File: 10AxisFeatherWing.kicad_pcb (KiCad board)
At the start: 2 copper layers, 50.8 x 22.9 mm, 28 parts, among them J1 feather long, J2 feather short, J4 feather long, J5 feather short, SW1 SW_Push_Dual, U1 BNO055, U2 BME280, Y1 32.768kHz

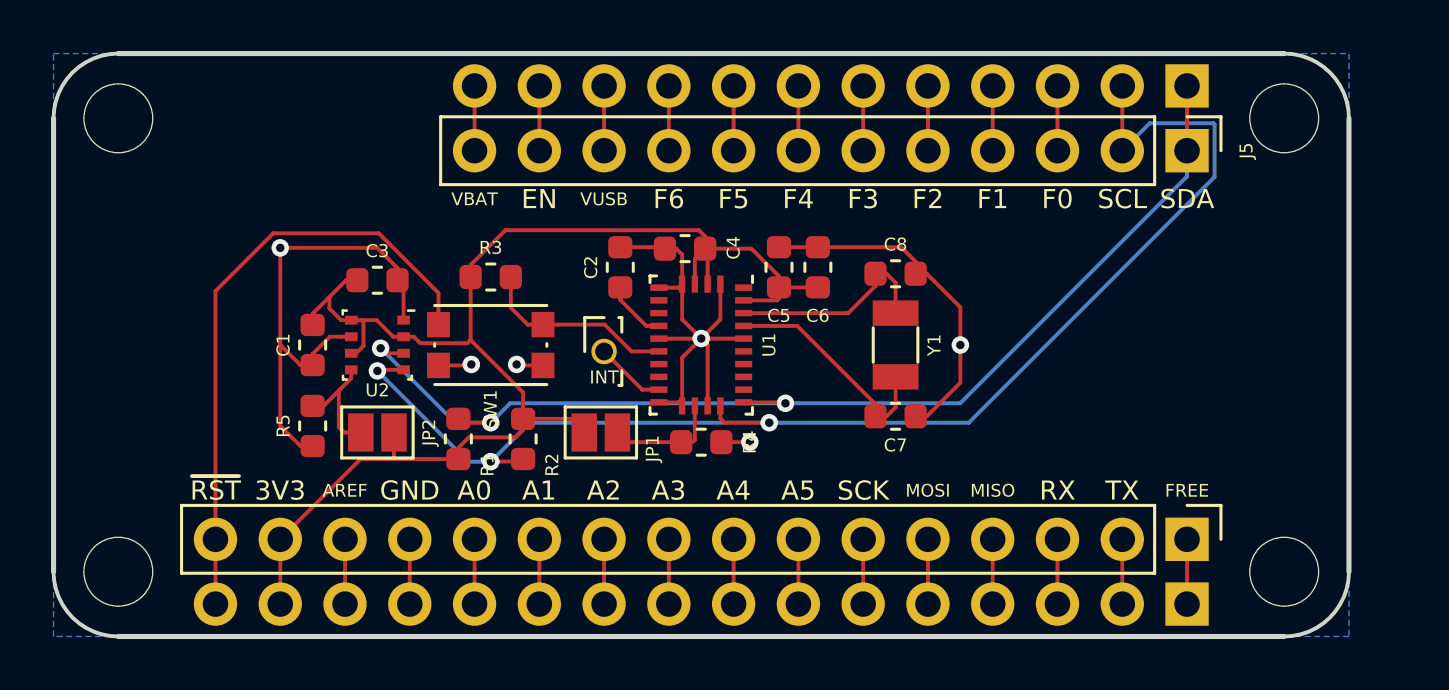
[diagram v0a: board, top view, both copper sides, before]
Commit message: Updated features
Replaced NRESET with pin instead of a button, Added silk text
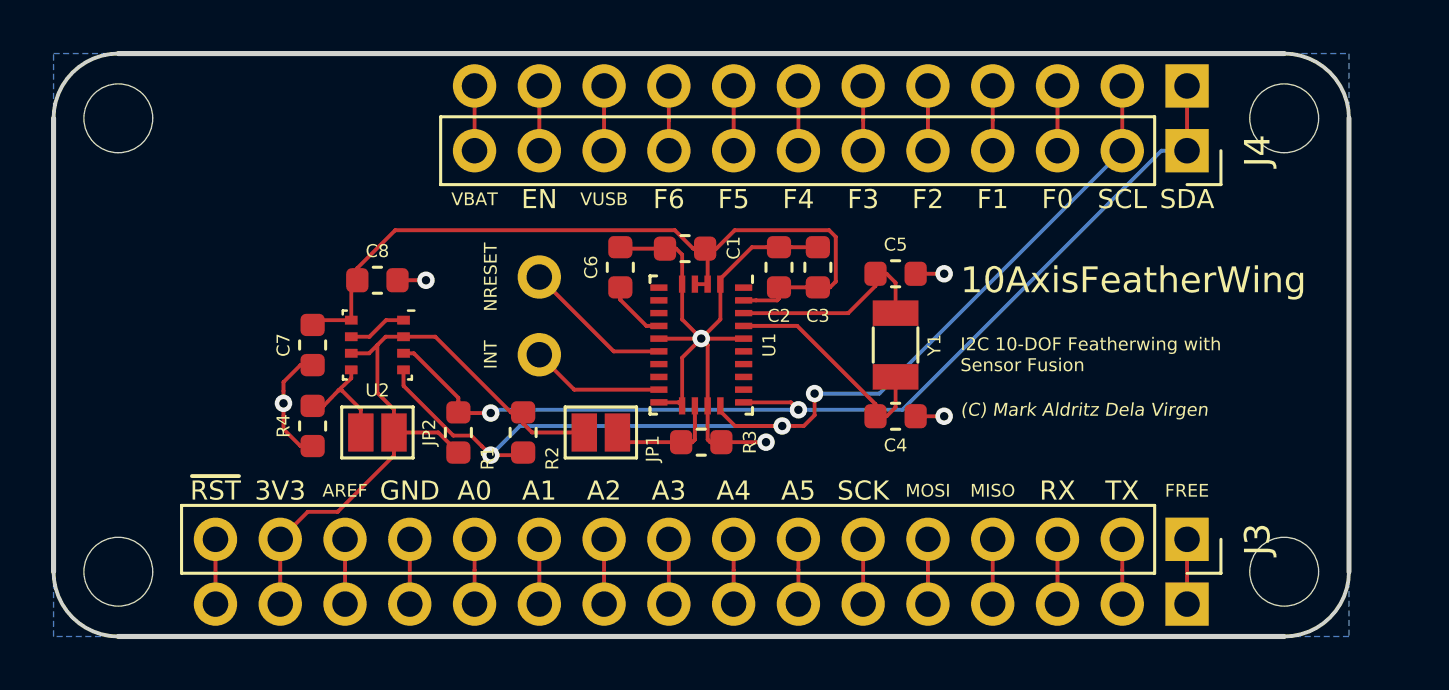
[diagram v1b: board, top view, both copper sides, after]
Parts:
- removed INT: INT, Connector_PinSocket_1.27mm:PinSocket_1x01_P1.27mm_Vertical
- removed the R3 at (42.5, 34.2)
- removed SW1: SW_Push_Dual, Button_Switch_SMD:SW_Push_1P1T_NO_CK_KMR2
- added J5: INT, Connector_Wire:SolderWirePad_1x01_Drill0.8mm, F.Cu at (44.5, 37.2)
- added J6: NRESET, Connector_Wire:SolderWirePad_1x01_Drill0.8mm, F.Cu at (44.5, 34.2)
- J3: renamed from J4; footprint Connector_PinHeader_2.54mm:PinHeader_1x16_P2.54mm_Vertical -> Connector_PinSocket_2.54mm:PinSocket_1x16_P2.54mm_Vertical
- J4: renamed from J5; footprint Connector_PinHeader_2.54mm:PinHeader_1x12_P2.54mm_Vertical -> Connector_PinSocket_2.54mm:PinSocket_1x12_P2.54mm_Vertical
- moved R1 0.25 mm to (41.3, 40.3)
- moved R2 0.25 mm to (43.8, 40.3)
- renumbered C4 to C1, C5 to C2, C6 to C3, C7 to C4, C8 to C5, C2 to C6, C1 to C7, C3 to C8, R4 to R3, R5 to R4
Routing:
- net /~RST: track 24.2 -> 2.54 mm
- net GND: track 58.7 -> 39.7 mm
- net /SCL: track 52.4 -> 42.1 mm
- net /SDA: track 44.4 -> 41.1 mm, vias 3 -> 2
- net /INT: track 2.77 -> 5.25 mm
- net +3V3: track 56.8 -> 58.7 mm
- net /NRESET: track 7.72 -> 5.90 mm
- net /SDO: track 5.20 -> 4.38 mm
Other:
- board text added: "(C) Mark Aldritz Dela Virgen"
- board text added: "10AxisFeatherWing"
- board text added: "I2C 10-DOF Featherwing with Sensor Fusion"
- board text added: "INT"
- board text added: "NRESET"

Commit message: Minor format fix
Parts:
- removed REF** (x4): MountingHole_2.7mm_M2.5, MountingHole:MountingHole_2.7mm_M2.5
- added H1: MountingHole, MountingHole:MountingHole_2.7mm_M2.5, F.Cu at (27.9, 27.9)
- added H2: MountingHole, MountingHole:MountingHole_2.7mm_M2.5, F.Cu at (27.9, 45.7)
- added H3: MountingHole, MountingHole:MountingHole_2.7mm_M2.5, F.Cu at (73.7, 27.9)
- added H4: MountingHole, MountingHole:MountingHole_2.7mm_M2.5, F.Cu at (73.7, 45.7)
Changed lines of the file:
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@@
     (add_net "Net-(U1-Pad8)")
+  )
+  (module MountingHole:MountingHole_2.7mm_M2.5 locked (layer F.Cu)
+    (at 73.66 45.72)
+    (descr "Mounting Hole 2.7mm, no annular, M2.5")
+    (tags "mounting hole 2.7mm no annular m2.5")
+    (attr virtual)
+    (fp_text reference H4 (at 0 -3.7) (layer F.SilkS) hide
+      (effects (font (size 1 1) (thickness 0.15)))
+    )
+    (fp_text value MountingHole (at 0 3.7) (layer F.Fab) hide
+      (effects (font (size 1 1) (thickness 0.15)))
+    )
+    (fp_circle (center 0 0) (end 2.95 0) (layer F.CrtYd) (width 0.05))
+    (fp_circle (center 0 0) (end 2.7 0) (layer Cmts.User) (width 0.15))
+    (fp_text user %R (at 0.3 0) (layer F.Fab)
+      (effects (font (size 1 1) (thickness 0.15)))
+    )
+    (pad 1 np_thru_hole circle (at 0 0) (size 2.7 2.7) (drill 2.7) (layers *.Cu *.Mask))
+  )
+  (module MountingHole:MountingHole_2.7mm_M2.5 locked (layer F.Cu)
+    (at 73.66 27.94)
+    (descr "Mounting Hole 2.7mm, no annular, M2.5")
+    (tags "mounting hole 2.7mm no annular m2.5")
+    (attr virtual)
+    (fp_text reference H3 (at 0 -3.7) (layer F.SilkS) hide
+      (effects (font (size 1 1) (thickness 0.15)))
+    )
+    (fp_text value MountingHole (at 0 3.7) (layer F.Fab) hide
+      (effects (font (size 1 1) (thickness 0.15)))
+    )
+    (fp_circle (center 0 0) (end 2.95 0) (layer F.CrtYd) (width 0.05))
+    (fp_circle (center 0 0) (end 2.7 0) (layer Cmts.User) (width 0.15))
+    (fp_text user %R (at 0.3 0) (layer F.Fab)
+      (effects (font (size 1 1) (thickness 0.15)))
+    )
+    (pad 1 np_thru_hole circle (at 0 0) (size 2.7 2.7) (drill 2.7) (layers *.Cu *.Mask))
+  )
+  (module MountingHole:MountingHole_2.7mm_M2.5 locked (layer F.Cu)
+    (at 27.94 45.72)
+    (descr "Mounting Hole 2.7mm, no annular, M2.5")
+    (tags "mounting hole 2.7mm no annular m2.5")
+    (attr virtual)
+    (fp_text reference H2 (at 0 -3.7) (layer F.SilkS) hide
+      (effects (font (size 1 1) (thickness 0.15)))
+    )
+    (fp_text value MountingHole (at 0 3.7) (layer F.Fab) hide
+      (effects (font (size 1 1) (thickness 0.15)))
+    )
+    (fp_circle (center 0 0) (end 2.95 0) (layer F.CrtYd) (width 0.05))
+    (fp_circle (center 0 0) (end 2.7 0) (layer Cmts.User) (width 0.15))
+    (fp_text user %R (at 0.3 0) (layer F.Fab)
+      (effects (font (size 1 1) (thickness 0.15)))
+    )
+    (pad 1 np_thru_hole circle (at 0 0) (size 2.7 2.7) (drill 2.7) (layers *.Cu *.Mask))
+  )
+  (module MountingHole:MountingHole_2.7mm_M2.5 locked (layer F.Cu)
+    (at 27.94 27.94)
+    (descr "Mounting Hole 2.7mm, no annular, M2.5")
+    (tags "mounting hole 2.7mm no annular m2.5")
+    (attr virtual)
+    (fp_text reference H1 (at 0 -3.7) (layer F.SilkS) hide
+      (effects (font (size 1 1) (thickness 0.15)))
+    )
+    (fp_text value MountingHole (at 0 3.7) (layer F.Fab) hide
+      (effects (font (size 1 1) (thickness 0.15)))
+    )
+    (fp_circle (center 0 0) (end 2.95 0) (layer F.CrtYd) (width 0.05))
+    (fp_circle (center 0 0) (end 2.7 0) (layer Cmts.User) (width 0.15))
+    (fp_text user %R (at 0.3 0) (layer F.Fab)
+      (effects (font (size 1 1) (thickness 0.15)))
+    )
+    (pad 1 np_thru_hole circle (at 0 0) (size 2.7 2.7) (drill 2.7) (layers *.Cu *.Mask))
   )
   (module Connector_Wire:SolderWirePad_1x01_Drill0.8mm (layer F.Cu)
@@
       (net 29 /INT))
   )
-  (module Connector_PinSocket_2.54mm:PinSocket_1x12_P2.54mm_Vertical (layer F.Cu)
+  (module Connector_PinSocket_2.54mm:PinSocket_1x12_P2.54mm_Vertical locked (layer F.Cu)
     (at 69.85 29.21 270)
     (descr "Through hole straight socket strip, 1x12, 2.54mm pitch, single row (from Kicad 4.0.7), script generated")
     (tags "Through hole socket strip THT 1x12 2.54mm single row")
-    (fp_text reference J4 (at 0 -2.77 90) (layer F.SilkS)
-      (effects (font (size 1 1) (thickness 0.15)))
-    )
-    (fp_text value "feather short" (at 0 30.71 90) (layer F.Fab)
+    (fp_text reference J4 (at 0 -2.77 90) (layer F.SilkS) hide
+      (effects (font (size 1 1) (thickness 0.15)))
+    )
+    (fp_text value "feather short" (at 0 30.71 90) (layer F.Fab) hide
       (effects (font (size 1 1) (thickness 0.15)))
     )
@@
     )
   )
-  (module Connector_PinSocket_2.54mm:PinSocket_1x16_P2.54mm_Vertical (layer F.Cu)
+  (module Connector_PinSocket_2.54mm:PinSocket_1x16_P2.54mm_Vertical locked (layer F.Cu)
     (at 69.85 44.45 270)
     (descr "Through hole straight socket strip, 1x16, 2.54mm pitch, single row (from Kicad 4.0.7), script generated")
     (tags "Through hole socket strip THT 1x16 2.54mm single row")
-    (fp_text reference J3 (at 0 -2.77 90) (layer F.SilkS)
-      (effects (font (size 1 1) (thickness 0.15)))
-    )
-    (fp_text value "feather long" (at 0 40.87 90) (layer F.Fab)
+    (fp_text reference J3 (at 0 -2.77 90) (layer F.SilkS) hide
+      (effects (font (size 1 1) (thickness 0.15)))
+    )
+    (fp_text value "feather long" (at 0 40.87 90) (layer F.Fab) hide
       (effects (font (size 1 1) (thickness 0.15)))
     )
@@
     )
   )
-  (module MountingHole:MountingHole_2.7mm_M2.5 locked (layer F.Cu)
-    (at 73.66 27.94)
-    (descr "Mounting Hole 2.7mm, no annular, M2.5")
-    (tags "mounting hole 2.7mm no annular m2.5")
-    (attr virtual)
-    (fp_text reference REF** (at 0 -3.7) (layer F.SilkS) hide
-      (effects (font (size 1 1) (thickness 0.15)))
-    )
-    (fp_text value MountingHole_2.7mm_M2.5 (at 0 3.7) (layer F.Fab) hide
-      (effects (font (size 1 1) (thickness 0.15)))
-    )
-    (fp_text user %R (at 0.3 0) (layer F.Fab) hide
-      (effects (font (size 1 1) (thickness 0.15)))
-    )
-    (fp_circle (center 0 0) (end 2.7 0) (layer Cmts.User) (width 0.15))
-    (fp_circle (center 0 0) (end 2.95 0) (layer F.CrtYd) (width 0.05))
-    (pad 1 np_thru_hole circle (at 0 0) (size 2.7 2.7) (drill 2.7) (layers *.Cu *.Mask))
-  )
-  (module MountingHole:MountingHole_2.7mm_M2.5 locked (layer F.Cu)
-    (at 73.66 45.72)
-    (descr "Mounting Hole 2.7mm, no annular, M2.5")
-    (tags "mounting hole 2.7mm no annular m2.5")
-    (attr virtual)
-    (fp_text reference REF** (at 0 -3.7) (layer F.SilkS) hide
-      (effects (font (size 1 1) (thickness 0.15)))
-    )
-    (fp_text value MountingHole_2.7mm_M2.5 (at 0 3.7) (layer F.Fab) hide
-      (effects (font (size 1 1) (thickness 0.15)))
-    )
-    (fp_circle (center 0 0) (end 2.95 0) (layer F.CrtYd) (width 0.05))
-    (fp_circle (center 0 0) (end 2.7 0) (layer Cmts.User) (width 0.15))
-    (fp_text user %R (at 0.3 0) (layer F.Fab) hide
-      (effects (font (size 1 1) (thickness 0.15)))
-    )
-    (pad 1 np_thru_hole circle (at 0 0) (size 2.7 2.7) (drill 2.7) (layers *.Cu *.Mask))
-  )
-  (module MountingHole:MountingHole_2.7mm_M2.5 locked (layer F.Cu)
-    (at 27.94 45.72)
-    (descr "Mounting Hole 2.7mm, no annular, M2.5")
-    (tags "mounting hole 2.7mm no annular m2.5")
-    (attr virtual)
-    (fp_text reference REF** (at 0 -3.7) (layer F.SilkS) hide
-      (effects (font (size 1 1) (thickness 0.15)))
-    )
-    (fp_text value MountingHole_2.7mm_M2.5 (at 0 3.7) (layer F.Fab) hide
-      (effects (font (size 1 1) (thickness 0.15)))
-    )
-    (fp_text user %R (at 0.3 0) (layer F.Fab) hide
-      (effects (font (size 1 1) (thickness 0.15)))
-    )
-    (fp_circle (center 0 0) (end 2.7 0) (layer Cmts.User) (width 0.15))
-    (fp_circle (center 0 0) (end 2.95 0) (layer F.CrtYd) (width 0.05))
-    (pad 1 np_thru_hole circle (at 0 0) (size 2.7 2.7) (drill 2.7) (layers *.Cu *.Mask))
-  )
-  (module MountingHole:MountingHole_2.7mm_M2.5 locked (layer F.Cu)
-    (at 27.94 27.94)
-    (descr "Mounting Hole 2.7mm, no annular, M2.5")
-    (tags "mounting hole 2.7mm no annular m2.5")
-    (attr virtual)
-    (fp_text reference REF** (at 0 -3.7) (layer F.SilkS) hide
-      (effects (font (size 1 1) (thickness 0.15)))
-    )
-    (fp_text value MountingHole_2.7mm_M2.5 (at 0 3.7) (layer F.Fab) hide
-      (effects (font (size 1 1) (thickness 0.15)))
-    )
-    (fp_circle (center 0 0) (end 2.95 0) (layer F.CrtYd) (width 0.05))
-    (fp_circle (center 0 0) (end 2.7 0) (layer Cmts.User) (width 0.15))
-    (fp_text user %R (at 0.3 0) (layer F.Fab) hide
-      (effects (font (size 1 1) (thickness 0.15)))
-    )
-    (pad 1 np_thru_hole circle (at 0 0) (size 2.7 2.7) (drill 2.7) (layers *.Cu *.Mask))
-  )
-  (module Connector_PinHeader_2.54mm:PinHeader_1x16_P2.54mm_Vertical (layer B.Cu)
+  (module Connector_PinHeader_2.54mm:PinHeader_1x16_P2.54mm_Vertical locked (layer B.Cu)
     (at 69.85 46.99 90)
     (descr "Through hole straight pin header, 1x16, 2.54mm pitch, single row")
@@
     )
   )
-  (module Connector_PinHeader_2.54mm:PinHeader_1x12_P2.54mm_Vertical (layer B.Cu)
+  (module Connector_PinHeader_2.54mm:PinHeader_1x12_P2.54mm_Vertical locked (layer B.Cu)
     (at 69.85 26.67 90)
     (descr "Through hole straight pin header, 1x12, 2.54mm pitch, single row")

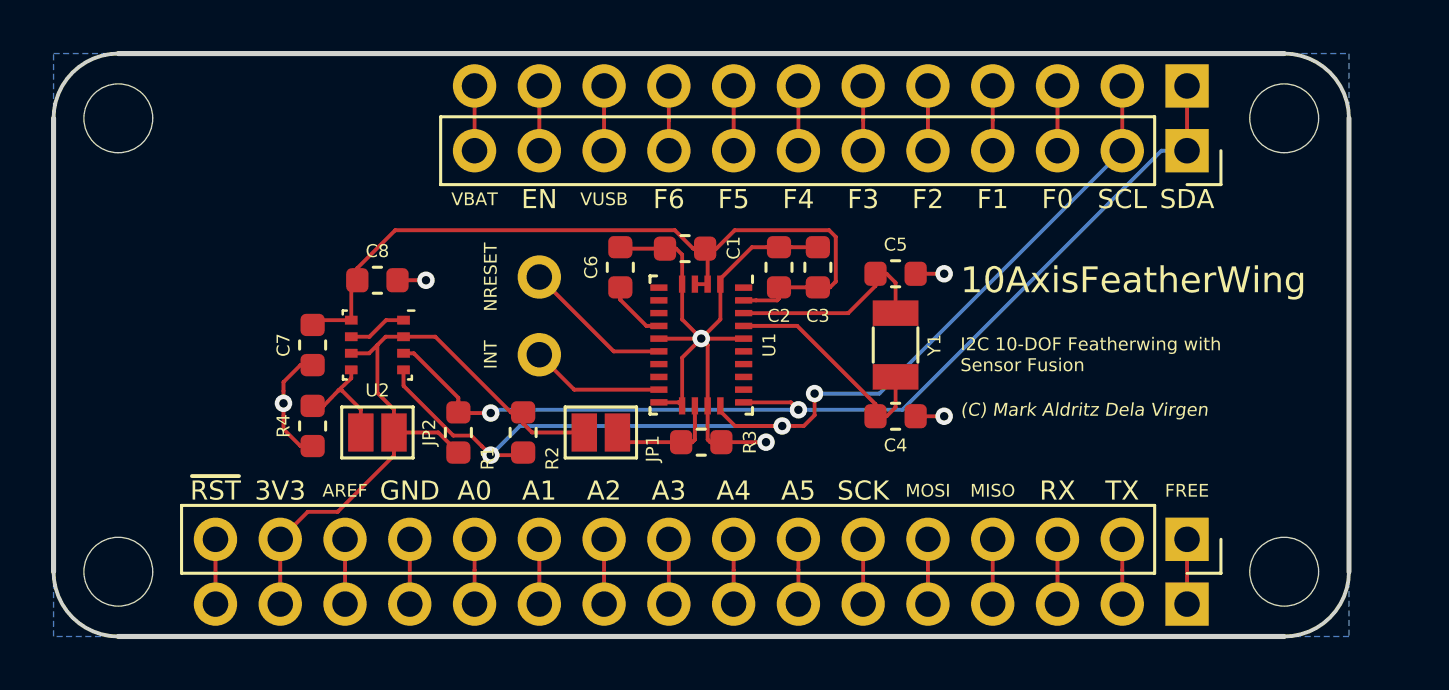
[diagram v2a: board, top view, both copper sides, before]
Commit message: Increased trace width
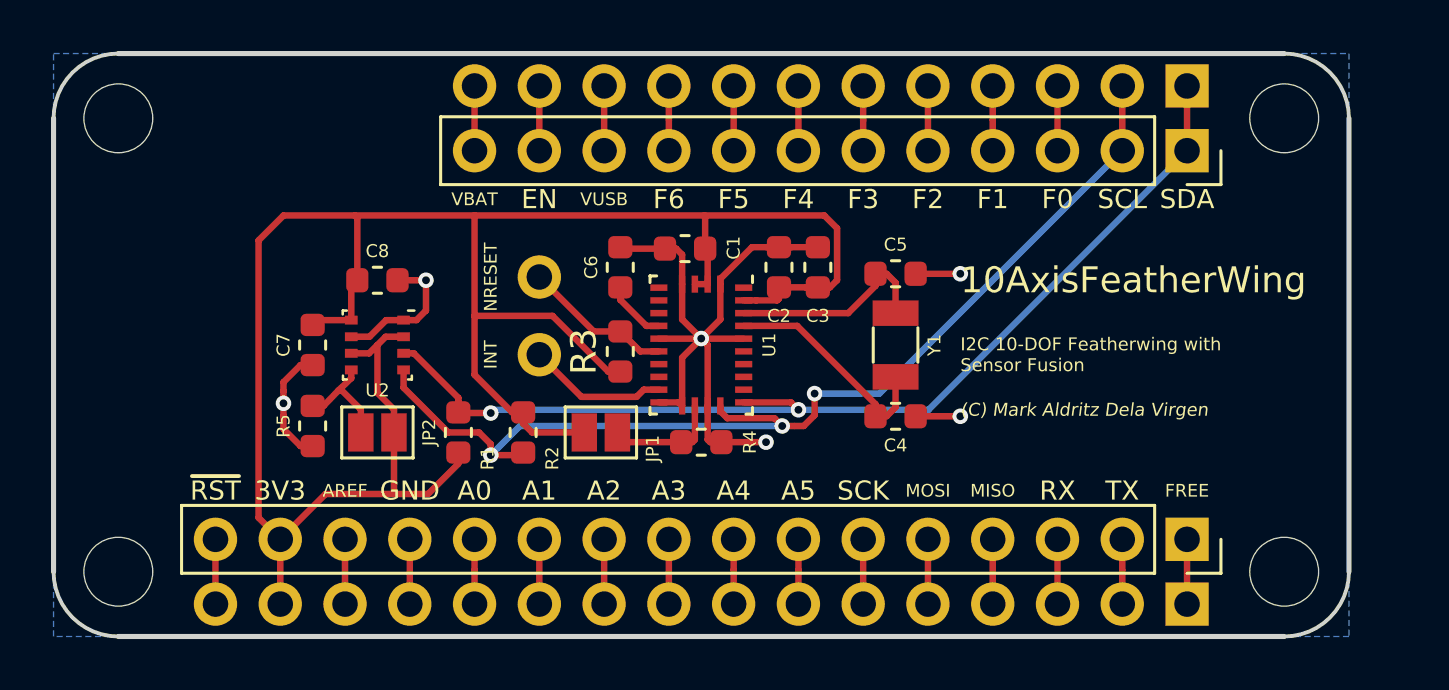
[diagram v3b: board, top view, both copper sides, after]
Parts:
- added R3: 10K, Resistor_SMD:R_0603_1608Metric, F.Cu at (47.6, 37.1)
- renumbered R3 to R4, R4 to R5
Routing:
- net +3V3: track 58.7 -> 88.7 mm
- net GND: track 39.7 -> 43.2 mm
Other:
- net class Default: trace_width 0.1524 -> 0.254; via_dia 0.6858 -> 0.6096; via_drill 0.3302 -> 0.3048

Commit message: Updated PCB
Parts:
- moved C4 4.32 mm to (54.6, 37.6)
- moved C5 4.32 mm to (54.6, 36.1)
- moved C2 1.08 mm to (54.6, 34.5), turned to 180 degrees
- moved C3 1.08 mm to (54.6, 33.0), turned to 180 degrees
- moved Y1 0.38 mm to (58.0, 36.8)
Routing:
- net GND: track 43.2 -> 39.3 mm, vias 6 -> 7
- net +3V3: track 88.7 -> 86.1 mm
- net Net-(C5-Pad1): track 8.21 -> 6.48 mm
- net Net-(C4-Pad2): track 9.04 -> 7.60 mm
- net /SDA: track 41.1 -> 42.2 mm
- net /SCL: track 42.4 -> 42.9 mm
